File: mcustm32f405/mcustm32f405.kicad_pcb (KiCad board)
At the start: 2 copper layers, 76.2 x 50.8 mm, 31 parts, among them J2 STM32WORLD_BASE, U1 AMS1117-3.3, U2 STM32F405RGTx, U3 SRV05-4, Y1 X_16MHZ

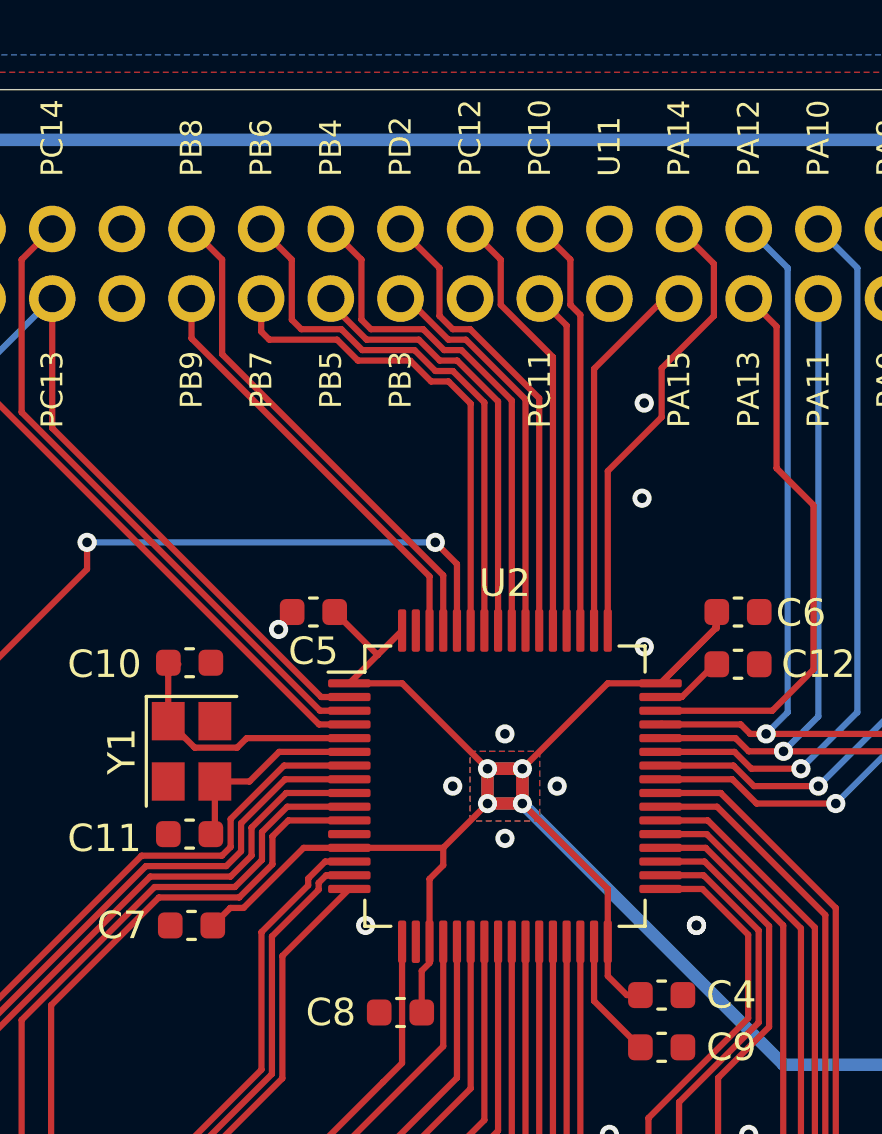
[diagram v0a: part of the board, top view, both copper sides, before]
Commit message: Created ioaw9523
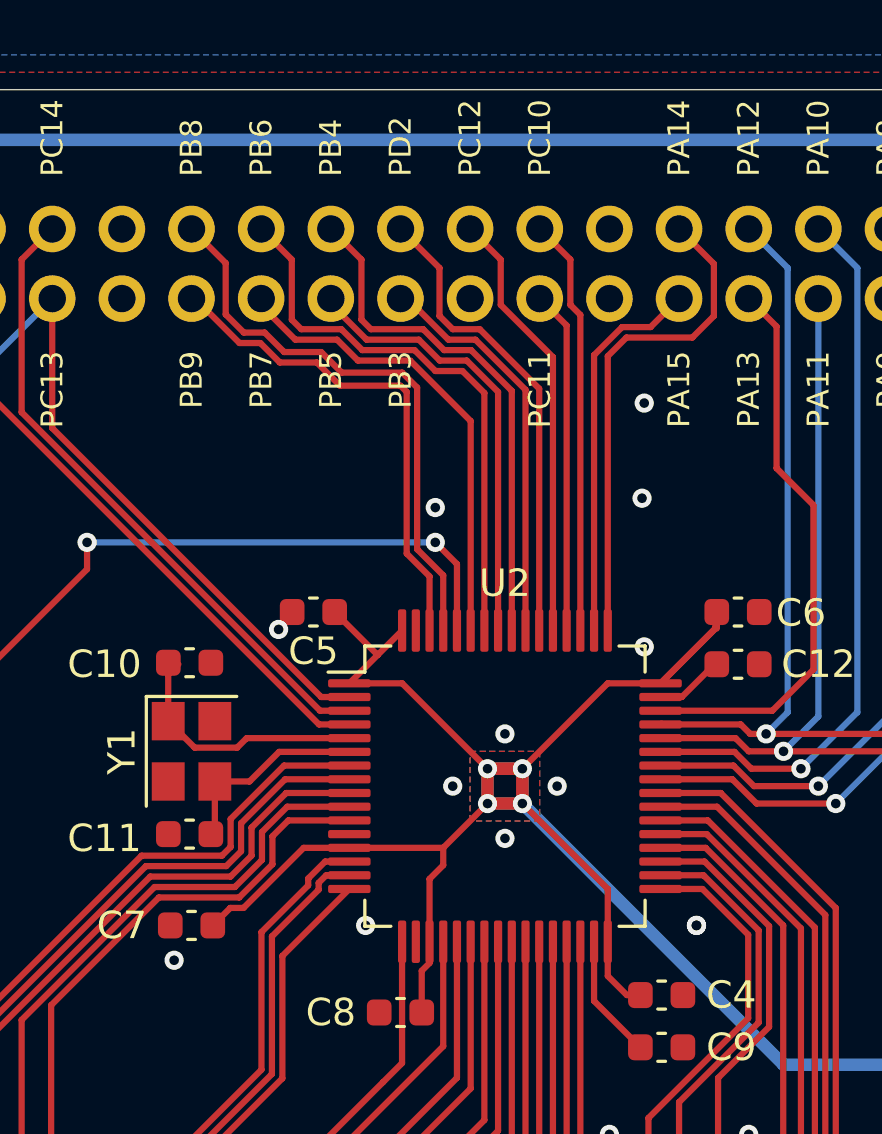
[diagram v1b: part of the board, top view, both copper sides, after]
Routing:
- net PB9: track 15.7 -> 18.3 mm
- net PB8: track 18.4 -> 21.0 mm
- net PA14: track 16.8 -> 18.2 mm
- net PB7: track 18.2 -> 17.3 mm
- net GND: vias 15 -> 17

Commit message: Added blank!
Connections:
- R3 pad 1: UCC -> PC14
- R4 pad 1: UCC -> PC14
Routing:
- net PC14: track 23.6 -> 60.7 mm, vias 0 -> 2
- net UCC: track 6.27 -> 0.00 mm

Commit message: Hmmm
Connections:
- J1 pad A8: Net-(J1-PadA8) -> unconnected-(J1-PadA8)
- J1 pad B8: Net-(J1-PadB8) -> unconnected-(J1-PadB8)
- J2 pad 22: Net-(J2-Pad22) -> unconnected-(J2-Pad22)
- J2 pad 33: Net-(J2-Pad33) -> unconnected-(J2-Pad33)
- J2 pad 34: Net-(J2-Pad34) -> unconnected-(J2-Pad34)
- J2 pad 35: Net-(J2-Pad35) -> unconnected-(J2-Pad35)
- J2 pad 36: Net-(J2-Pad36) -> unconnected-(J2-Pad36)
- J2 pad 45: Net-(J2-Pad45) -> unconnected-(J2-Pad45)
- J2 pad 46: Net-(J2-Pad46) -> unconnected-(J2-Pad46)
- J2 pad 47: Net-(J2-Pad47) -> unconnected-(J2-Pad47)
- J2 pad 48: Net-(J2-Pad48) -> unconnected-(J2-Pad48)
- J2 pad 57: Net-(J2-Pad57) -> unconnected-(J2-Pad57)
- J2 pad 58: Net-(J2-Pad58) -> unconnected-(J2-Pad58)
- J2 pad 62: Net-(J2-Pad62) -> unconnected-(J2-Pad62)
- J2 pad 71: Net-(J2-Pad71) -> unconnected-(J2-Pad71)
- J2 pad 72: Net-(J2-Pad72) -> unconnected-(J2-Pad72)
- J2 pad 75: Net-(J2-Pad75) -> unconnected-(J2-Pad75)
- J2 pad 77: Net-(J2-Pad77) -> unconnected-(J2-Pad77)
- J2 pad 78: Net-(J2-Pad78) -> unconnected-(J2-Pad78)
- U3 pad 4: Net-(U3-Pad4) -> unconnected-(U3-Pad4)
- U3 pad 6: Net-(U3-Pad6) -> unconnected-(U3-Pad6)
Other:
- net class Default removed

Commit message: Hmmmm
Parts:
- added C2: C_100NF_0603, Capacitor_SMD:C_0603_1608Metric, F.Cu at (145.4, 95.2)
- added C8: C_100NF_0603, Capacitor_SMD:C_0603_1608Metric, F.Cu at (141.0, 106.0)
- added FB1: FB_0603, Inductor_SMD:L_0603_1608Metric, F.Cu at (141.0, 108.0)
- added JP1: SolderJumper_2_Bridged, Jumper:SolderJumper-2_P1.3mm_Bridged_RoundedPad1.0x1.5mm, B.Cu at (144.8, 99.7)
- added JP2: SolderJumper_2_Bridged, Jumper:SolderJumper-2_P1.3mm_Bridged_RoundedPad1.0x1.5mm, B.Cu at (144.8, 104.8)
- moved C7 17.3 mm to (158.1, 109.2), turned to 0 degrees
- moved C12 1.91 mm to (158.1, 113.0)
- moved C4 1.91 mm to (158.1, 111.1)
- moved C5 1.91 mm to (145.4, 93.3)
- moved Y1 1.91 mm to (141.0, 98.4)
- moved C11 1.85 mm to (140.9, 95.2)
- moved C13 1.75 mm to (141.0, 101.6)
- renumbered C2 to C10, C10 to C11, C9 to C12, C11 to C13, C12 to C14, C8 to C9, R3 to R1, R4 to R2, R5 to R3, R6 to R4, R1 to R5, R2 to R6, U3 to U2, U2 to U3
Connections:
- J2 pad 1: +3V3 -> VDDA
- J2 pad 79: +3V3 -> VBAT
- U3 pad 1: +3V3 -> VBAT
- U3 pad 13: +3V3 -> VA
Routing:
- net +3V3: track 280.8 -> 206.1 mm, vias 14 -> 15
- net VBAT: track 0.00 -> 37.9 mm, vias 0 -> 2
- net VDDA: track 0.00 -> 27.2 mm, vias 0 -> 1
- net VA: track 0.00 -> 7.88 mm
- net BO0: track 61.9 -> 58.3 mm
- net Net-(C12-Pad1): track 4.55 -> 6.46 mm
- net PC15: track 21.7 -> 23.2 mm
- net PC3: track 24.1 -> 25.3 mm
- net PC14: track 60.7 -> 61.8 mm
- net PC2: track 28.0 -> 29.1 mm
- net PC1: track 26.1 -> 27.2 mm
- net PC0: track 30.1 -> 31.2 mm
- net NRST: track 42.7 -> 43.5 mm
- net PA1: track 19.2 -> 18.5 mm
- net VBUS: track 13.6 -> 14.3 mm
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
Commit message: Hmmmm
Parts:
- SW1, SW2: value ~ -> TS-1088R-02526
- renumbered C9 to C10, C10 to C9
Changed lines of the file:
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@@
     )
     (pad_to_mask_clearance 0)
-    (aux_axis_origin 111.125 130.175)
-    (grid_origin 111.125 130.175)
+    (aux_axis_origin 98.425 136.525)
+    (grid_origin 98.425 136.525)
     (pcbplotparams
       (layerselection 0x00010fc_ffffffff)
@@
       (viasonmask false)
       (mode 1)
-      (useauxorigin false)
+      (useauxorigin true)
       (hpglpennumber 1)
       (hpglpenspeed 20)
@@
       (outputformat 1)
       (mirror false)
-      (drillshape 1)
+      (drillshape 0)
       (scaleselection 1)
-      (outputdirectory "")
+      (outputdirectory "rev_a/")
     )
   )
@@
     )
   )
-  (footprint "stm32world:TS-1088R-02526" (layer "F.Cu")
-    (at 118.11 116.205)
-    (property "LCSC" "C455281")
-    (property "Sheetfile" "mcustm32f405.kicad_sch")
-    (property "Sheetname" "")
-    (attr through_hole)
-    (fp_text reference "SW1" (at 0 0) (layer "F.SilkS")
-      (effects (font (size 1 1) (thickness 0.15)))
-    )
-    (fp_text value "~" (at 0 2.8) (layer "F.Fab")
-      (effects (font (size 1 1) (thickness 0.15)))
-    )
-    (fp_line (start 2.7 1.8) (end -2.7 1.8) (layer "F.SilkS") (width 0.15))
-    (fp_line (start -2.7 -1.8) (end 2.7 -1.8) (layer "F.SilkS") (width 0.15))
-    (fp_line (start -2 -1.5) (end 2 -1.5) (layer "F.Fab") (width 0.12))
-    (fp_line (start 2 -1.5) (end 2 1.5) (layer "F.Fab") (width 0.12))
-    (fp_line (start 2 1.5) (end -2 1.5) (layer "F.Fab") (width 0.12))
-    (fp_line (start -2 1.5) (end -2 -1.5) (layer "F.Fab") (width 0.12))
-    (fp_circle (center 0 0) (end 0.5 -1) (layer "F.Fab") (width 0.12) (fill none))
-    (pad "1" smd rect locked (at -2.2 -0.05) (size 1.2 2) (layers "F.Cu" "F.Paste" "F.Mask")
-      (net 2 "GND") (pinfunction "1") (pintype "passive"))
-    (pad "2" smd rect locked (at 2.2 0) (size 1.2 2) (layers "F.Cu" "F.Paste" "F.Mask")
-      (net 49 "NRST") (pinfunction "2") (pintype "passive"))
-    (model "${KIPRJMOD}/../lib/3x4x2 tact button.step"
-      (offset (xyz -2.5 0.75 0))
-      (scale (xyz 1 1 1))
-      (rotate (xyz -90 0 0))
-    )
-  )
-  (footprint "stm32world:TS-1088R-02526" (layer "F.Cu")
-    (at 118.11 110.49 180)
-    (property "LCSC" "C455281")
-    (property "Sheetfile" "mcustm32f405.kicad_sch")
-    (property "Sheetname" "")
-    (attr through_hole)
-    (fp_text reference "SW2" (at 0 0) (layer "F.SilkS")
-      (effects (font (size 1 1) (thickness 0.15)))
-    )
-    (fp_text value "~" (at 0 2.8) (layer "F.Fab")
-      (effects (font (size 1 1) (thickness 0.15)))
-    )
-    (fp_line (start -2.7 -1.8) (end 2.7 -1.8) (layer "F.SilkS") (width 0.15))
-    (fp_line (start 2.7 1.8) (end -2.7 1.8) (layer "F.SilkS") (width 0.15))
-    (fp_line (start -2 -1.5) (end 2 -1.5) (layer "F.Fab") (width 0.12))
-    (fp_line (start 2 -1.5) (end 2 1.5) (layer "F.Fab") (width 0.12))
-    (fp_line (start 2 1.5) (end -2 1.5) (layer "F.Fab") (width 0.12))
-    (fp_line (start -2 1.5) (end -2 -1.5) (layer "F.Fab") (width 0.12))
-    (fp_circle (center 0 0) (end 0.5 -1) (layer "F.Fab") (width 0.12) (fill none))
-    (pad "1" smd rect locked (at -2.2 -0.05 180) (size 1.2 2) (layers "F.Cu" "F.Paste" "F.Mask")
-      (net 58 "BO0") (pinfunction "1") (pintype "passive"))
-    (pad "2" smd rect locked (at 2.2 0 180) (size 1.2 2) (layers "F.Cu" "F.Paste" "F.Mask")
-      (net 1 "+3V3") (pinfunction "2") (pintype "passive"))
-    (model "${KIPRJMOD}/../lib/3x4x2 tact button.step"
-      (offset (xyz -2.5 0.75 0))
-      (scale (xyz 1 1 1))
-      (rotate (xyz -90 0 0))
-    )
-  )
   (footprint "Capacitor_SMD:C_0603_1608Metric" (layer "F.Cu")
     (at 145.415 93.345 180)
@@
     (property "Sheetname" "")
     (attr smd)
-    (fp_text reference "C9" (at 2.54 0) (layer "F.SilkS")
+    (fp_text reference "C10" (at 2.54 0) (layer "F.SilkS")
       (effects (font (size 1 1) (thickness 0.15)))
     )
@@
     (property "Sheetname" "")
     (attr smd)
-    (fp_text reference "C10" (at 2.58 -0.07) (layer "F.SilkS")
+    (fp_text reference "C9" (at 2.58 -0.07) (layer "F.SilkS")
       (effects (font (size 1 1) (thickness 0.15)))
     )
@@
     )
   )
+  (footprint "stm32world:TS-1088R-02526" (layer "F.Cu")
+    (at 118.11 116.205)
+    (property "LCSC" "C455281")
+    (property "Sheetfile" "mcustm32f405.kicad_sch")
+    (property "Sheetname" "")
+    (attr through_hole)
+    (fp_text reference "SW1" (at 0 0) (layer "F.SilkS")
+      (effects (font (size 1 1) (thickness 0.15)))
+    )
+    (fp_text value "TS-1088R-02526" (at 0 2.8) (layer "F.Fab")
+      (effects (font (size 1 1) (thickness 0.15)))
+    )
+    (fp_line (start 2.7 1.8) (end -2.7 1.8) (layer "F.SilkS") (width 0.15))
+    (fp_line (start -2.7 -1.8) (end 2.7 -1.8) (layer "F.SilkS") (width 0.15))
+    (fp_line (start 2 -1.5) (end 2 1.5) (layer "F.Fab") (width 0.12))
+    (fp_line (start 2 1.5) (end -2 1.5) (layer "F.Fab") (width 0.12))
+    (fp_line (start -2 -1.5) (end 2 -1.5) (layer "F.Fab") (width 0.12))
+    (fp_line (start -2 1.5) (end -2 -1.5) (layer "F.Fab") (width 0.12))
+    (fp_circle (center 0 0) (end 0.5 -1) (layer "F.Fab") (width 0.12) (fill none))
+    (pad "1" smd rect (at -2.2 -0.05) (size 1.2 2) (layers "F.Cu" "F.Paste" "F.Mask")
+      (net 2 "GND") (pinfunction "1") (pintype "passive"))
+    (pad "2" smd rect (at 2.2 0) (size 1.2 2) (layers "F.Cu" "F.Paste" "F.Mask")
+      (net 49 "NRST") (pinfunction "2") (pintype "passive"))
+    (model "${KIPRJMOD}/../lib/3x4x2 tact button.step"
+      (offset (xyz -2.5 0.75 0))
+      (scale (xyz 1 1 1))
+      (rotate (xyz -90 0 0))
+    )
+  )
+  (footprint "stm32world:TS-1088R-02526" (layer "F.Cu")
+    (at 118.11 110.49 180)
+    (property "LCSC" "C455281")
+    (property "Sheetfile" "mcustm32f405.kicad_sch")
+    (property "Sheetname" "")
+    (attr through_hole)
+    (fp_text reference "SW2" (at 0 0) (layer "F.SilkS")
+      (effects (font (size 1 1) (thickness 0.15)))
+    )
+    (fp_text value "TS-1088R-02526" (at 0 2.8) (layer "F.Fab")
+      (effects (font (size 1 1) (thickness 0.15)))
+    )
+    (fp_line (start 2.7 1.8) (end -2.7 1.8) (layer "F.SilkS") (width 0.15))
+    (fp_line (start -2.7 -1.8) (end 2.7 -1.8) (layer "F.SilkS") (width 0.15))
+    (fp_line (start 2 -1.5) (end 2 1.5) (layer "F.Fab") (width 0.12))
+    (fp_line (start -2 -1.5) (end 2 -1.5) (layer "F.Fab") (width 0.12))
+    (fp_line (start -2 1.5) (end -2 -1.5) (layer "F.Fab") (width 0.12))
+    (fp_line (start 2 1.5) (end -2 1.5) (layer "F.Fab") (width 0.12))
+    (fp_circle (center 0 0) (end 0.5 -1) (layer "F.Fab") (width 0.12) (fill none))
+    (pad "1" smd rect (at -2.2 -0.05 180) (size 1.2 2) (layers "F.Cu" "F.Paste" "F.Mask")
+      (net 58 "BO0") (pinfunction "1") (pintype "passive"))
+    (pad "2" smd rect (at 2.2 0 180) (size 1.2 2) (layers "F.Cu" "F.Paste" "F.Mask")
+      (net 1 "+3V3") (pinfunction "2") (pintype "passive"))
+    (model "${KIPRJMOD}/../lib/3x4x2 tact button.step"
+      (offset (xyz -2.5 0.75 0))
+      (scale (xyz 1 1 1))
+      (rotate (xyz -90 0 0))
+    )
+  )
